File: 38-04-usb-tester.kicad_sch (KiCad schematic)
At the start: 63 parts, among them J1 USB3_A, J2 B_USB_B_Micro, J3 10137061-00021LF, J4 B_USB_B_Mini, J5 Conn_01x05_Pin, J6 10137061-00021LF, SW1 SW_SPDT, U1 STM32C031K6Tx

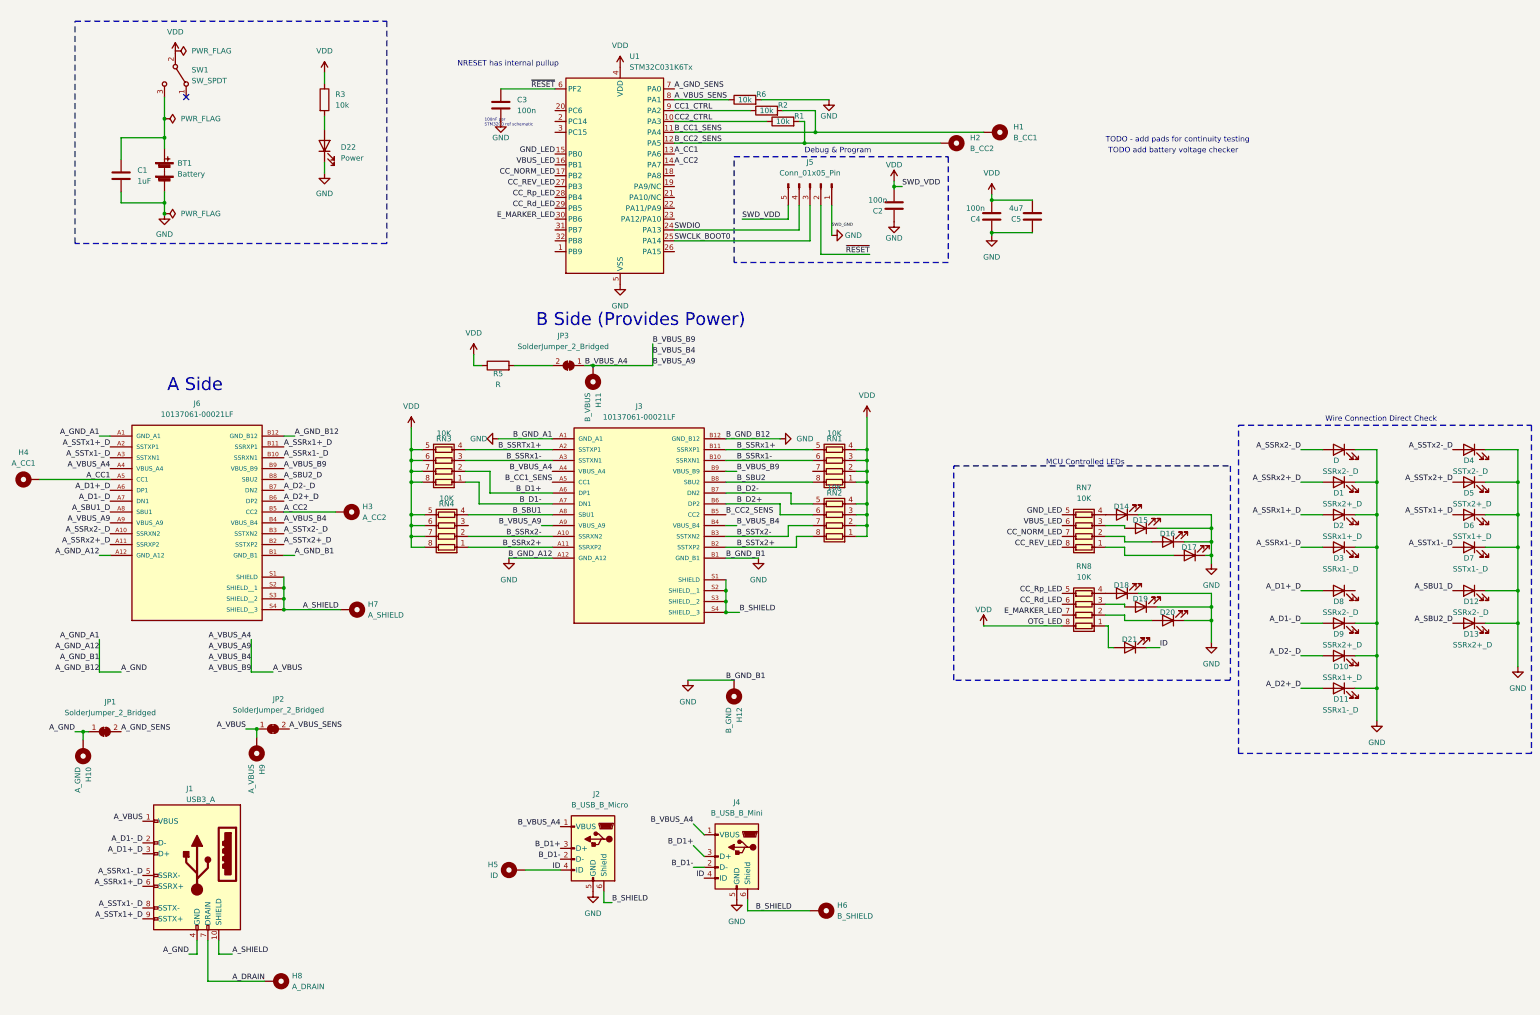
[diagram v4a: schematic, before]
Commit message: added new footprints, schematic edits
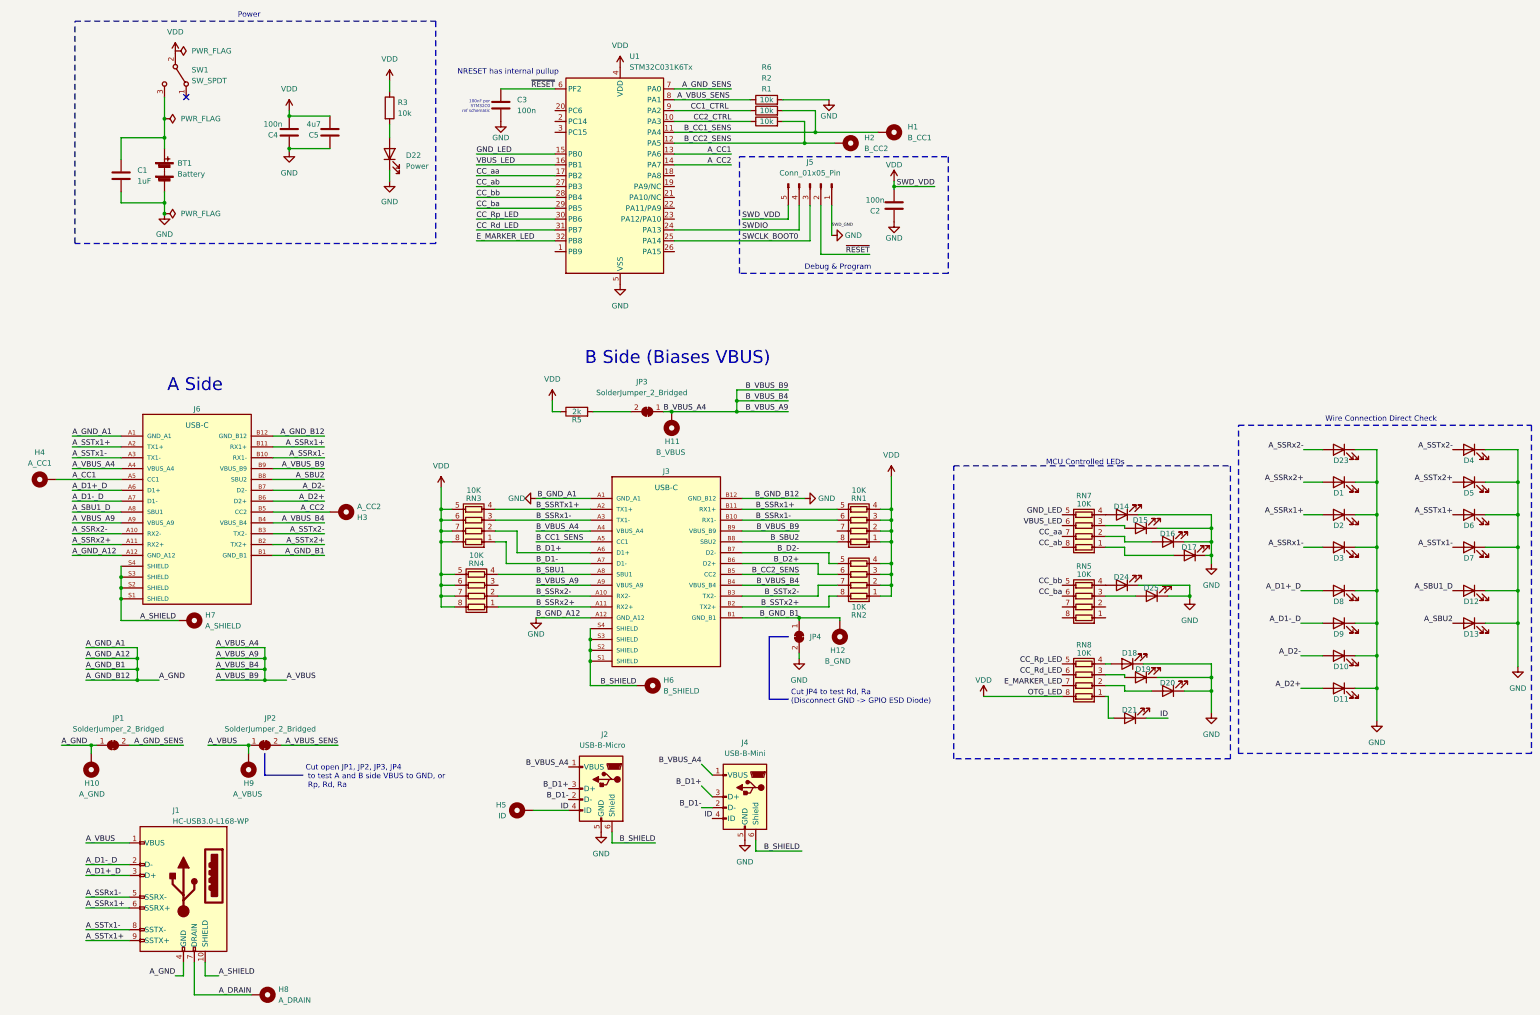
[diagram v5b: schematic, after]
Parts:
- added D24: CC_bb_D, LED_SMD:LED_0805_2012Metric, symbol Device:LED
- added D25: CC_ba_D, LED_SMD:LED_0805_2012Metric, symbol Device:LED
- added JP4: SolderJumper_2_Bridged, Jumper:SolderJumper-2_P1.3mm_Open_RoundedPad1.0x1.5mm, symbol Jumper:SolderJumper_2_Bridged
- added RN5: 10K, Resistor_SMD:R_Array_Concave_4x0402, symbol Device:R_Pack04
- C2, C3, C4, C5: footprint (none) -> Capacitor_SMD:C_0805_2012Metric
- D14: value ~ -> GND_D
- D15: value ~ -> VBUS_LED_D
- D16: value ~ -> CC_NORM_D
- D17: value ~ -> CC_REV_D
- D18: value ~ -> Rp_D
- D19: value ~ -> Rd_D
- D20: value ~ -> Ra_D
- D21: value ~ -> OTG_D
- D22: footprint (none) -> LED_SMD:LED_0805_2012Metric
- H1, H10, H11, H12, H2, H3, H4, H5, H6, H7, H8, H9: footprint (none) -> MountingHole:MountingHole_2.5mm_Pad_TopBottom
- J1: value USB3_A -> HC-USB3.0-L168-WP; footprint Connector_USB:USB3_A_Molex_48393-001 -> 01-UserLibary:HC-USB3.0-L168-WP_USB-A_THT-9-2MP_P2.0mm; JLPCB_MPN (none) -> HC-USB3.0-L168-WP; JLPCB_Mfg (none) -> Hong Cheng; JLPCB_Part_No (none) -> C7501850; JLPCB_URL (none) -> https://jlcpcb.com/partdetail/HongCheng-HC_USB3_0_L168WP/C7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
- J2: value B_USB_B_Micro -> USB-B-Micro; footprint Connector_USB:USB_Micro-B_Molex-105017-0001 -> 01-UserLibary:USB_Micro-B_Kinghelm-KH-MICRO5P-JN; JLPCB_MPN (none) -> KH-MICRO5P-JN; JLPCB_Mfg (none) -> Shenzhen Kinghelm Elec; JLPCB_Part_No (none) -> C962222; JLPCB_URL (none) -> https://jlcpcb.com/partdetail/Shenzhen_KinghelmElec-KH_MICR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
- J3: value 10137061-00021LF -> USB-C; footprint EXT_usb-c-10137061_00021LF:AMPHENOL_10137061-00021LF -> 12401832E402A:AMPHENOL_12401832E402A; symbol SM_usb-c-10137061_00021LF:10137061-00021LF -> EXT_usb-c-AMPHENOL-12401832E402A:12401832E402A; Check_prices (none) -> https://www.snapeda.com/parts/12401832E402A/Amphenol+FCI/vi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; DigiKey_Part_Number (none) -> 12401832E402ATR-ND; MANUFACTURER Amphenol FCI -> Amphenol; MAXIMUM_PACKAGE_HIEGHT (none) -> 3.28mm; MF (none) -> Amphenol ICC; MP (none) -> 12401832E402A; PARTREV C -> X2; Package (none) -> None; Purchase-URL (none) -> https://www.snapeda.com/api/url_track_click_mouser/?unipart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; STANDARD Manufacturer recommendations -> Manufacturer Recommendations; SnapEDA_Link (none) -> https://www.snapeda.com/parts/12401832E402A/Amphenol+FCI/vi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
- J4: value B_USB_B_Mini -> USB-B-Mini
- J5: footprint (none) -> Connector_PinSocket_2.54mm:PinSocket_1x05_P2.54mm_Vertical
- J6: value 10137061-00021LF -> USB-C; footprint EXT_usb-c-10137061_00021LF:AMPHENOL_10137061-00021LF -> (none); symbol SM_usb-c-10137061_00021LF:10137061-00021LF -> EXT_usb-c-AMPHENOL-12401832E402A:12401832E402A; Check_prices (none) -> https://www.snapeda.com/parts/12401832E402A/Amphenol+FCI/vi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; DigiKey_Part_Number (none) -> 12401832E402ATR-ND; MANUFACTURER Amphenol FCI -> Amphenol; MAXIMUM_PACKAGE_HIEGHT (none) -> 3.28mm; MF (none) -> Amphenol ICC; MP (none) -> 12401832E402A; PARTREV C -> X2; Package (none) -> None; Purchase-URL (none) -> https://www.snapeda.com/api/url_track_click_mouser/?unipart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; STANDARD Manufacturer recommendations -> Manufacturer Recommendations; SnapEDA_Link (none) -> https://www.snapeda.com/parts/12401832E402A/Amphenol+FCI/vi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
- JP1, JP2, JP3: footprint (none) -> Jumper:SolderJumper-2_P1.3mm_Open_RoundedPad1.0x1.5mm
- R1, R2, R3, R6: footprint (none) -> Resistor_SMD:R_0201_0603Metric
- R5: value R -> 2k; footprint (none) -> Jumper:SolderJumper-2_P1.3mm_Open_RoundedPad1.0x1.5mm
- RN1, RN2, RN3, RN4, RN7, RN8: footprint (none) -> Resistor_SMD:R_Array_Concave_4x0402
- renumbered D to D23
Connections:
- net CC_Rd_LED: now also U1.31 (PB7); no longer U1.29 (PB5)
- net CC_Rp_LED: now also U1.30 (PB6); no longer U1.28 (PB4)
- net E_MARKER_LED: now also U1.32 (PB8); no longer U1.30 (PB6)
- net GND: now also D8.1 (K), D24.1 (K), D25.1 (K), JP4.2 (B); no longer H12.1, J3.B1 (GND_B1)
- net A_D2+_D renamed A_D2+
- net A_D2-_D renamed A_D2-
- net A_SBU2_D renamed A_SBU2
- net A_SSRx1+_D renamed A_SSRx1+
- net A_SSRx1-_D renamed A_SSRx1-
- net A_SSRx2+_D renamed A_SSRx2+
- net A_SSRx2-_D renamed A_SSRx2-
- net A_SSTx1+_D renamed A_SSTx1+
- net A_SSTx1-_D renamed A_SSTx1-
- net A_SSTx2+_D renamed A_SSTx2+
- net A_SSTx2-_D renamed A_SSTx2-
- net CC_NORM_LED renamed CC_aa
- net CC_REV_LED renamed CC_ab
- new net: D25.2 (A), RN5.3 (R3.1)
- new net: D24.2 (A), RN5.4 (R4.1)
- new net B_GND_B1: H12.1, J3.B1 (GND_B1), JP4.1 (A)
- new net CC_ba: RN5.6 (R3.2), U1.29 (PB5)
- new net CC_bb: RN5.5 (R4.2), U1.28 (PB4)
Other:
- note added: "B Side (Biases VBUS)"
- note added: "Cut JP4 to test Rd, Ra (Disconnect GND -> GPIO ESD Diode)"
- note added: "Cut open JP1, JP2, JP3, JP4 to test A and B side VBUS to GND, or Rp, Rd, Ra"
- note added: "Power"
- note removed: "B Side (Provides Power)"
- note removed: "TODO - add pads for continuity testing"
- note removed: "TODO add battery voltage checker"
- moved on the sheet: C4, C5, D18, D19, D20, D21, D22, H1, H10, H11, H12, H2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

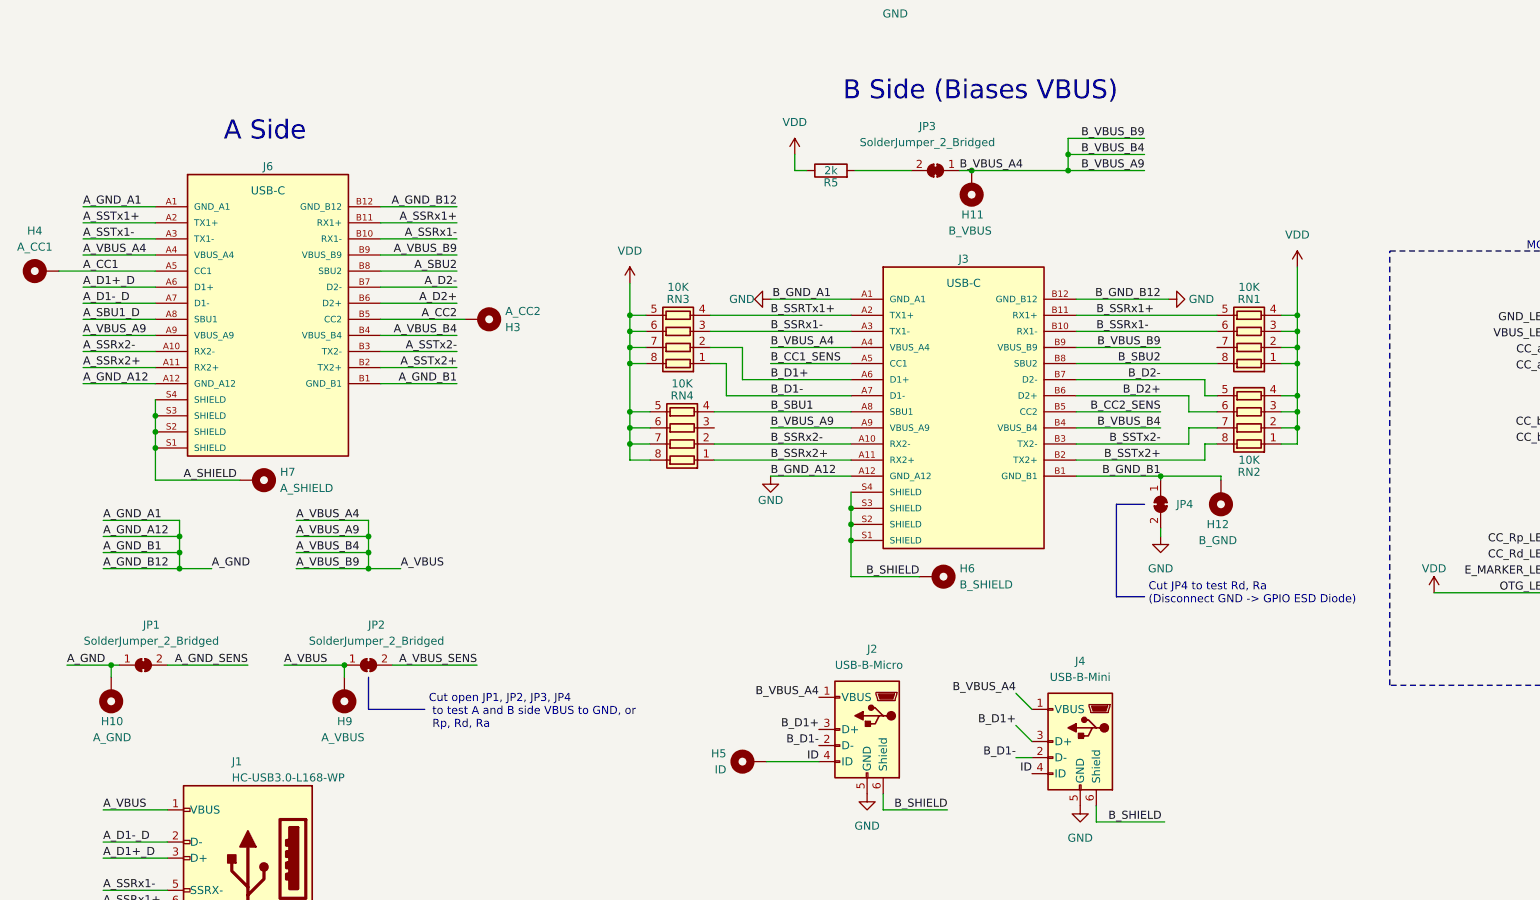
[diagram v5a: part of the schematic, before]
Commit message: mini b and dip switch footprint and schems
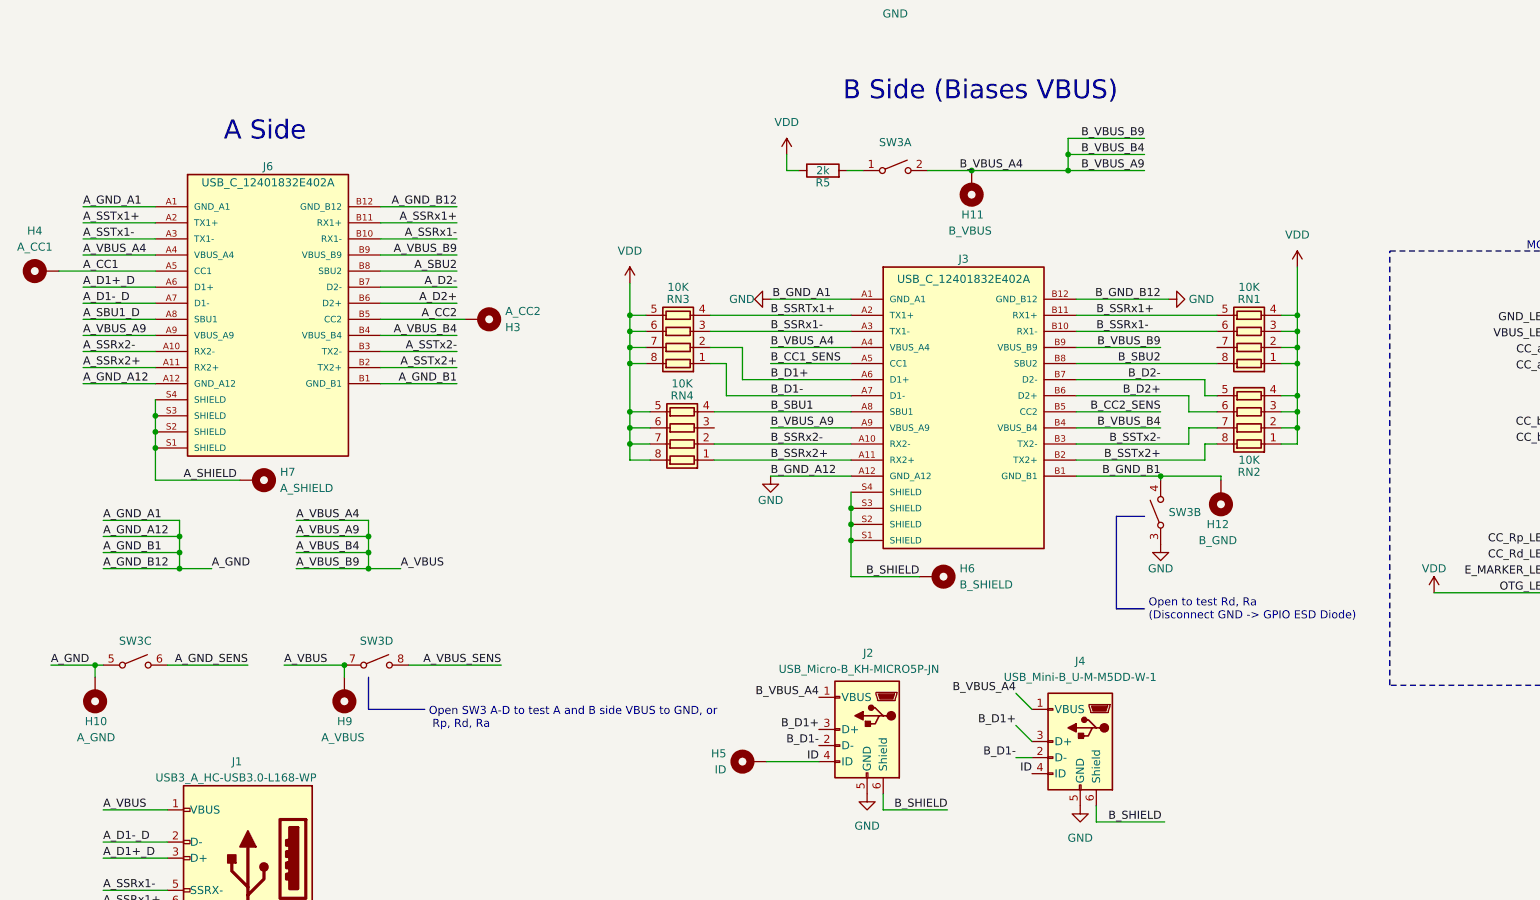
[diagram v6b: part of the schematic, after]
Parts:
- removed JP1, JP2, JP3, JP4: SolderJumper_2_Bridged, Jumper:SolderJumper-2_P1.3mm_Open_RoundedPad1.0x1.5mm, symbol Jumper:SolderJumper_2_Bridged
- added SW3: ~, 01-UserLibary:SW-DIP-4P_P1.27mm_SMD-2x4, symbol 01B-UserSchematics:SW_DIP_x04_Separated
- J1: value HC-USB3.0-L168-WP -> USB3_A_HC-USB3.0-L168-WP
- J2: value USB-B-Micro -> USB_Micro-B_KH-MICRO5P-JN
- J3: value USB-C -> USB_C_12401832E402A; footprint 12401832E402A:AMPHENOL_12401832E402A -> 01-UserLibary:USB_C_Receptacle_Amphenol_12401832E402A; JLPCB_MPN (none) -> 12401832E402A; JLPCB_Mfg (none) -> Amphenol ICC; JLPCB_Part_No (none) -> C464604; JLPCB_URL (none) -> https://jlcpcb.com/partdetail/AmphenolIcc-12401832E402A/C46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
- J4: value USB-B-Mini -> USB_Mini-B_U-M-M5DD-W-1; footprint Connector_USB:USB_Mini-B_Wuerth_65100516121_Horizontal -> 01-UserLibary:USB_Mini-B_Korean-Hroparts_U-M-M5DD-W-1_SMD-5-4MP; JLPCB_MPN (none) -> U-M-M5DD-W-1; JLPCB_Mfg (none) -> Korean Hroparts Elec; JLPCB_Part_No (none) -> C145778; JLPCB_URL (none) -> https://jlcpcb.com/partdetail/Korean_HropartsElec-U_M_M5DD_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
- J6: value USB-C -> USB_C_12401832E402A; footprint (none) -> 01-UserLibary:USB_C_Receptacle_Amphenol_12401832E402A; JLPCB_MPN (none) -> 12401832E402A; JLPCB_Mfg (none) -> Amphenol ICC; JLPCB_Part_No (none) -> C464604; JLPCB_URL (none) -> https://jlcpcb.com/partdetail/AmphenolIcc-12401832E402A/C46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
- R5: footprint Jumper:SolderJumper-2_P1.3mm_Open_RoundedPad1.0x1.5mm -> (none)
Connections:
- net A_GND: now also SW3.5
- net A_GND_SENS: now also SW3.6
- net A_VBUS: now also SW3.7
- net A_VBUS_SENS: now also SW3.8
- net B_GND_B1: now also SW3.4
- net B_VBUS_A4: now also SW3.2
- net GND: now also SW3.3
- net at R5.2: now also SW3.1
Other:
- note added: "Open SW3 A-D to test A and B side VBUS to GND, or Rp, Rd, Ra"
- note added: "Open to test Rd, Ra (Disconnect GND -> GPIO ESD Diode)"
- note removed: "Cut JP4 to test Rd, Ra (Disconnect GND -> GPIO ESD Diode)"
- note removed: "Cut open JP1, JP2, JP3, JP4 to test A and B side VBUS to GND, or Rp, Rd, Ra"
- moved on the sheet: H10, R5
